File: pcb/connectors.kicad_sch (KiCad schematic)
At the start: 5 parts, among them J1 GPIO, J2 Hirose_FH12-16S, J3 TC2030

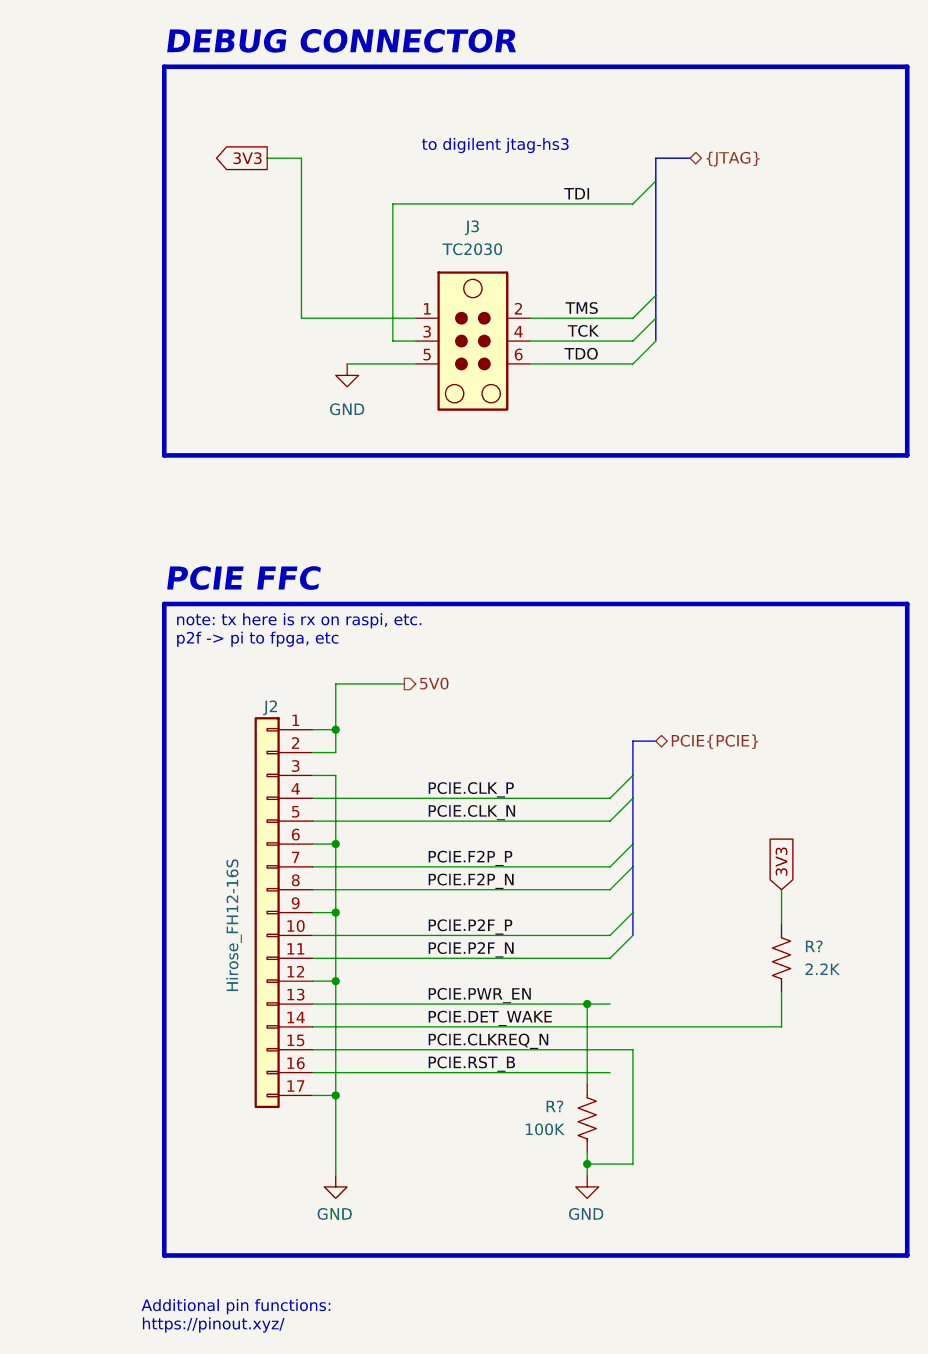
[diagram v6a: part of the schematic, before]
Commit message: added dram, defined pcie sideband sigs.
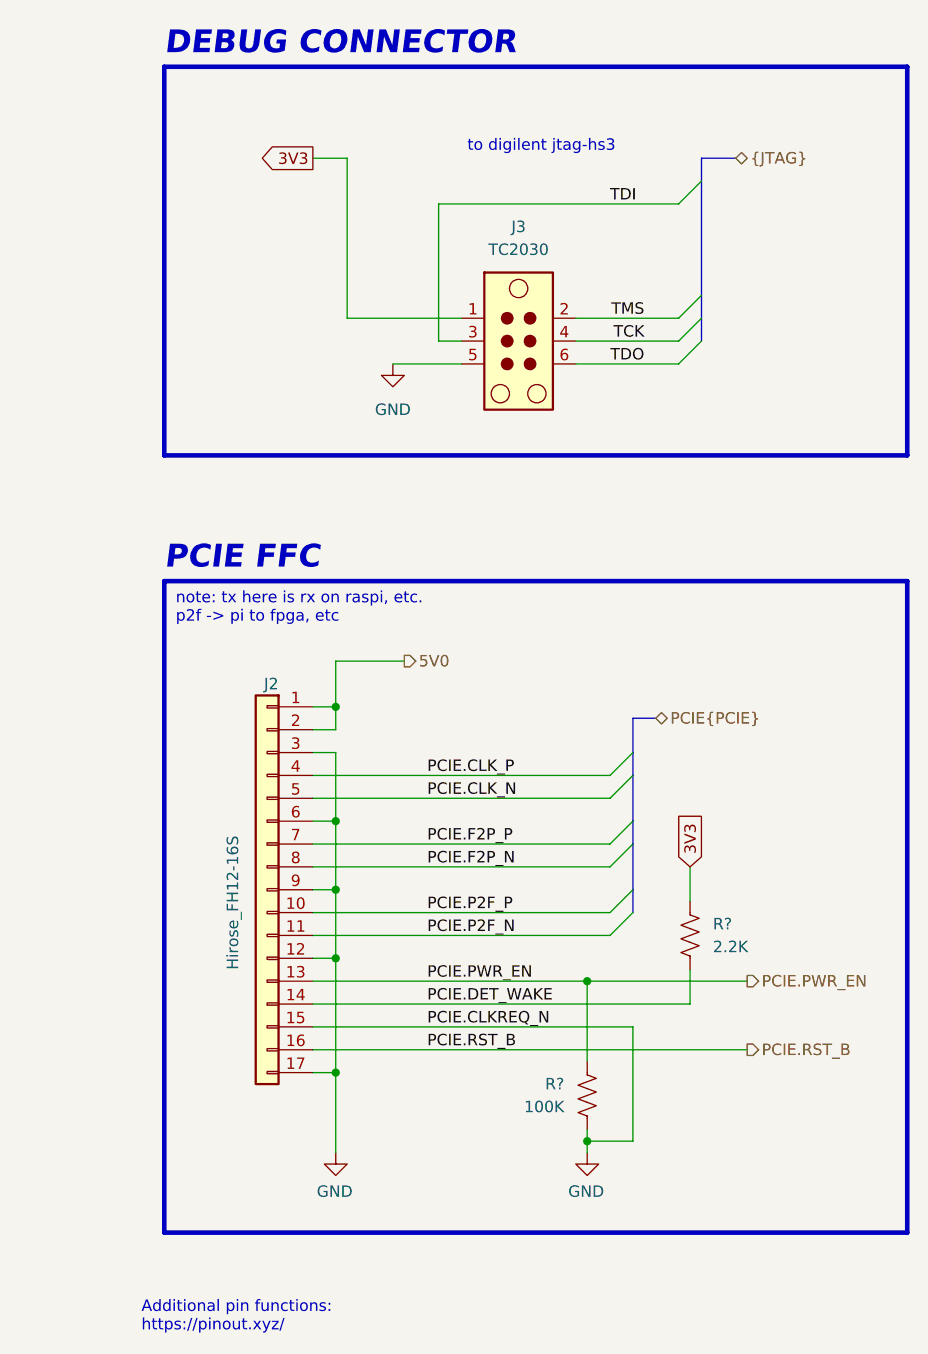
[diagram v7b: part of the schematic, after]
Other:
- moved on the sheet: J2, J3, R?

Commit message: ddr3
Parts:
- gave numbers to parts that had none: 2
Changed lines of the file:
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@@
 		(dnp no)
 		(fields_autoplaced yes)
-		(property "Reference" "R?"
+		(property "Reference" "R25"
 			(at 241.3 125.7299 0)
 			(effects
@@
 			(project ""
 				(path "/e63e39d7-6ac0-4ffd-8aa3-1841a4541b55/6418cef5-c0d2-4573-8432-9553c4202f1e"
-					(reference "R?")
+					(reference "R25")
 					(unit 1)
 				)
@@
 		(on_board yes)
 		(dnp no)
-		(property "Reference" "R?"
+		(property "Reference" "R24"
 			(at 224.79 143.51 0)
 			(effects
@@
 			(project "RPi-HwAB-1"
 				(path "/e63e39d7-6ac0-4ffd-8aa3-1841a4541b55/6418cef5-c0d2-4573-8432-9553c4202f1e"
-					(reference "R?")
+					(reference "R24")
 					(unit 1)
 				)
